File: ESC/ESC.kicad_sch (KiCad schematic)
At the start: 121 parts, among them J1 Screw_Terminal_01x02, J2 Conn_01x05, J3 Screw_Terminal_01x03, Q1 BS250, Q2 IPD031N03L, Q3 IPD031N03L, Q4 IPD031N03L, Q5 IPD031N03L, Q6 IPD031N03L, Q7 IPD031N03L, U1 LM7805_TO220, U2 DRV8302, U3 IR2101, U5 IR2101, U6 IR2101

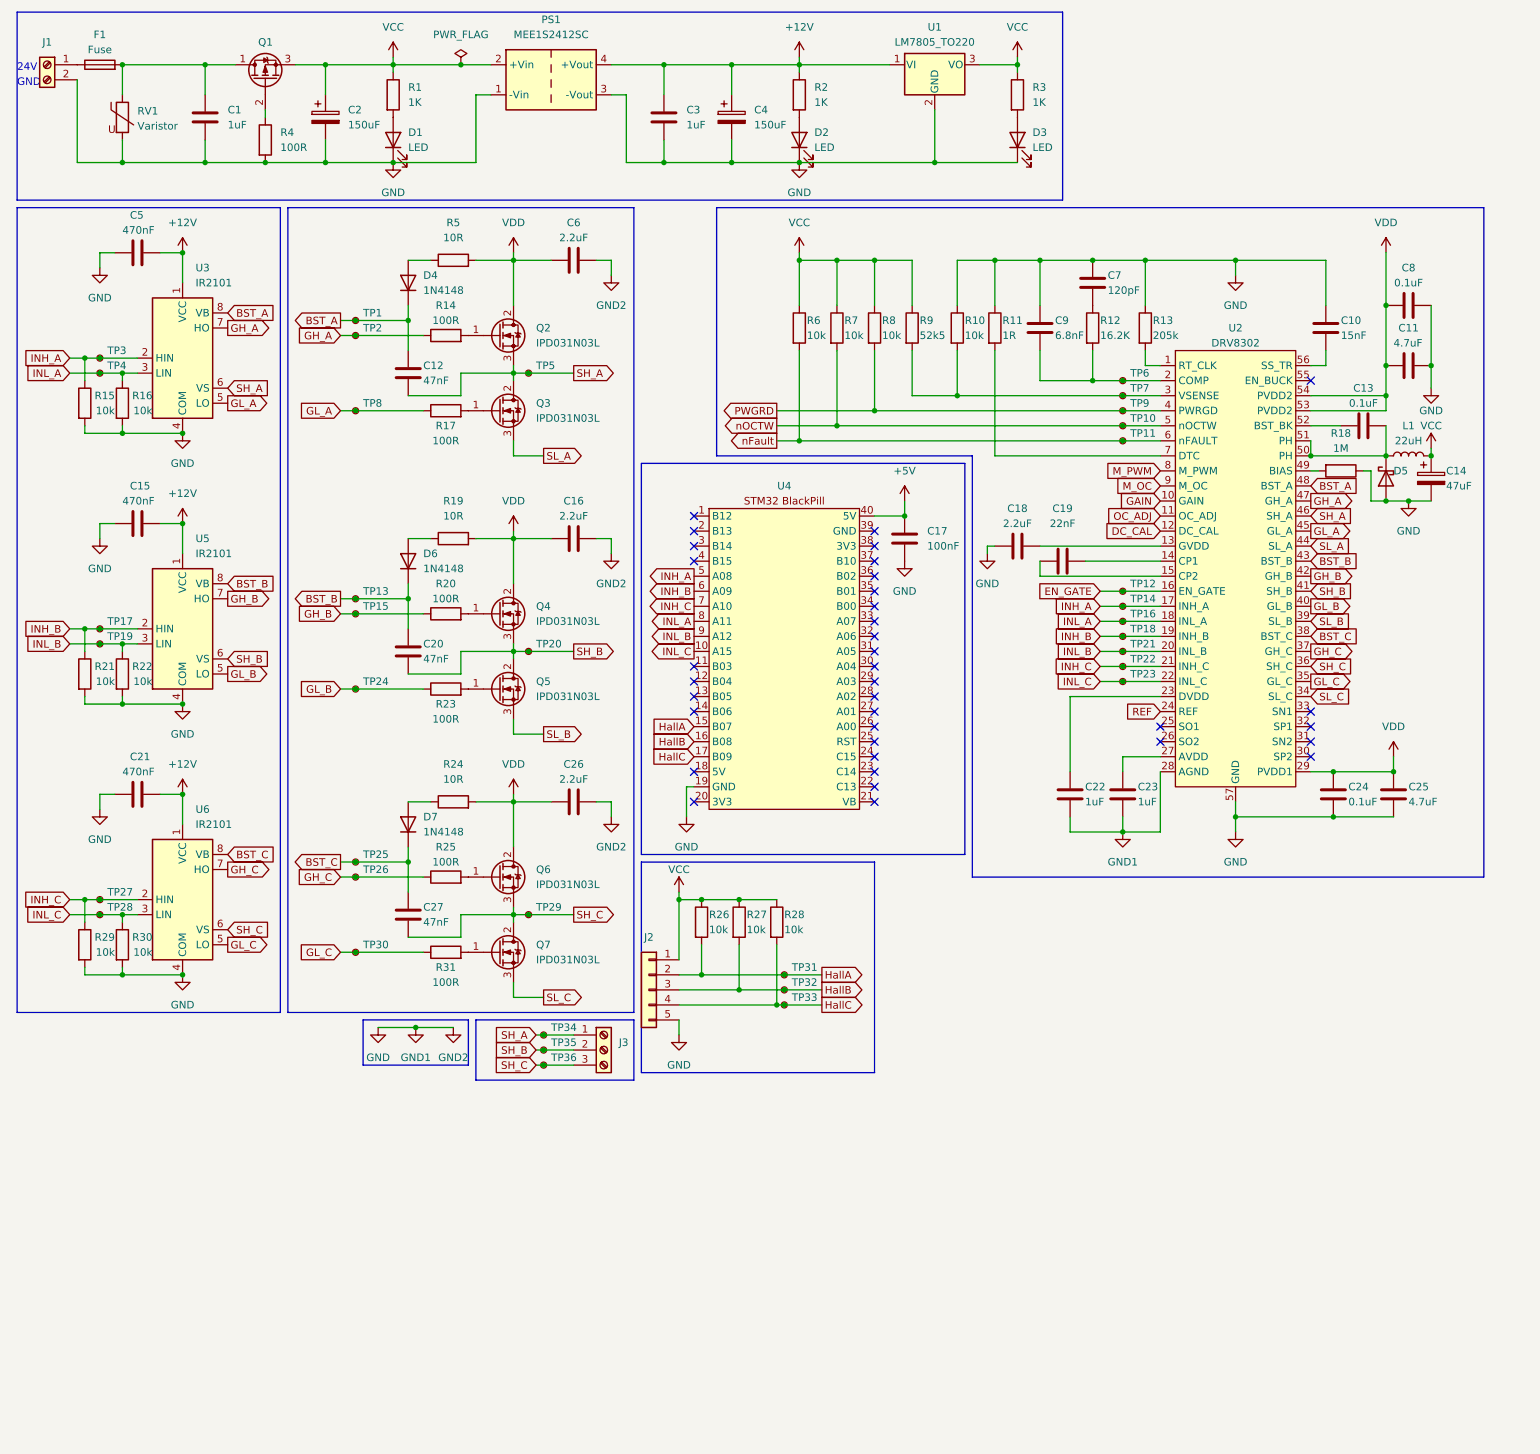
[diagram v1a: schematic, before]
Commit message: Added Connectors SPI and USART
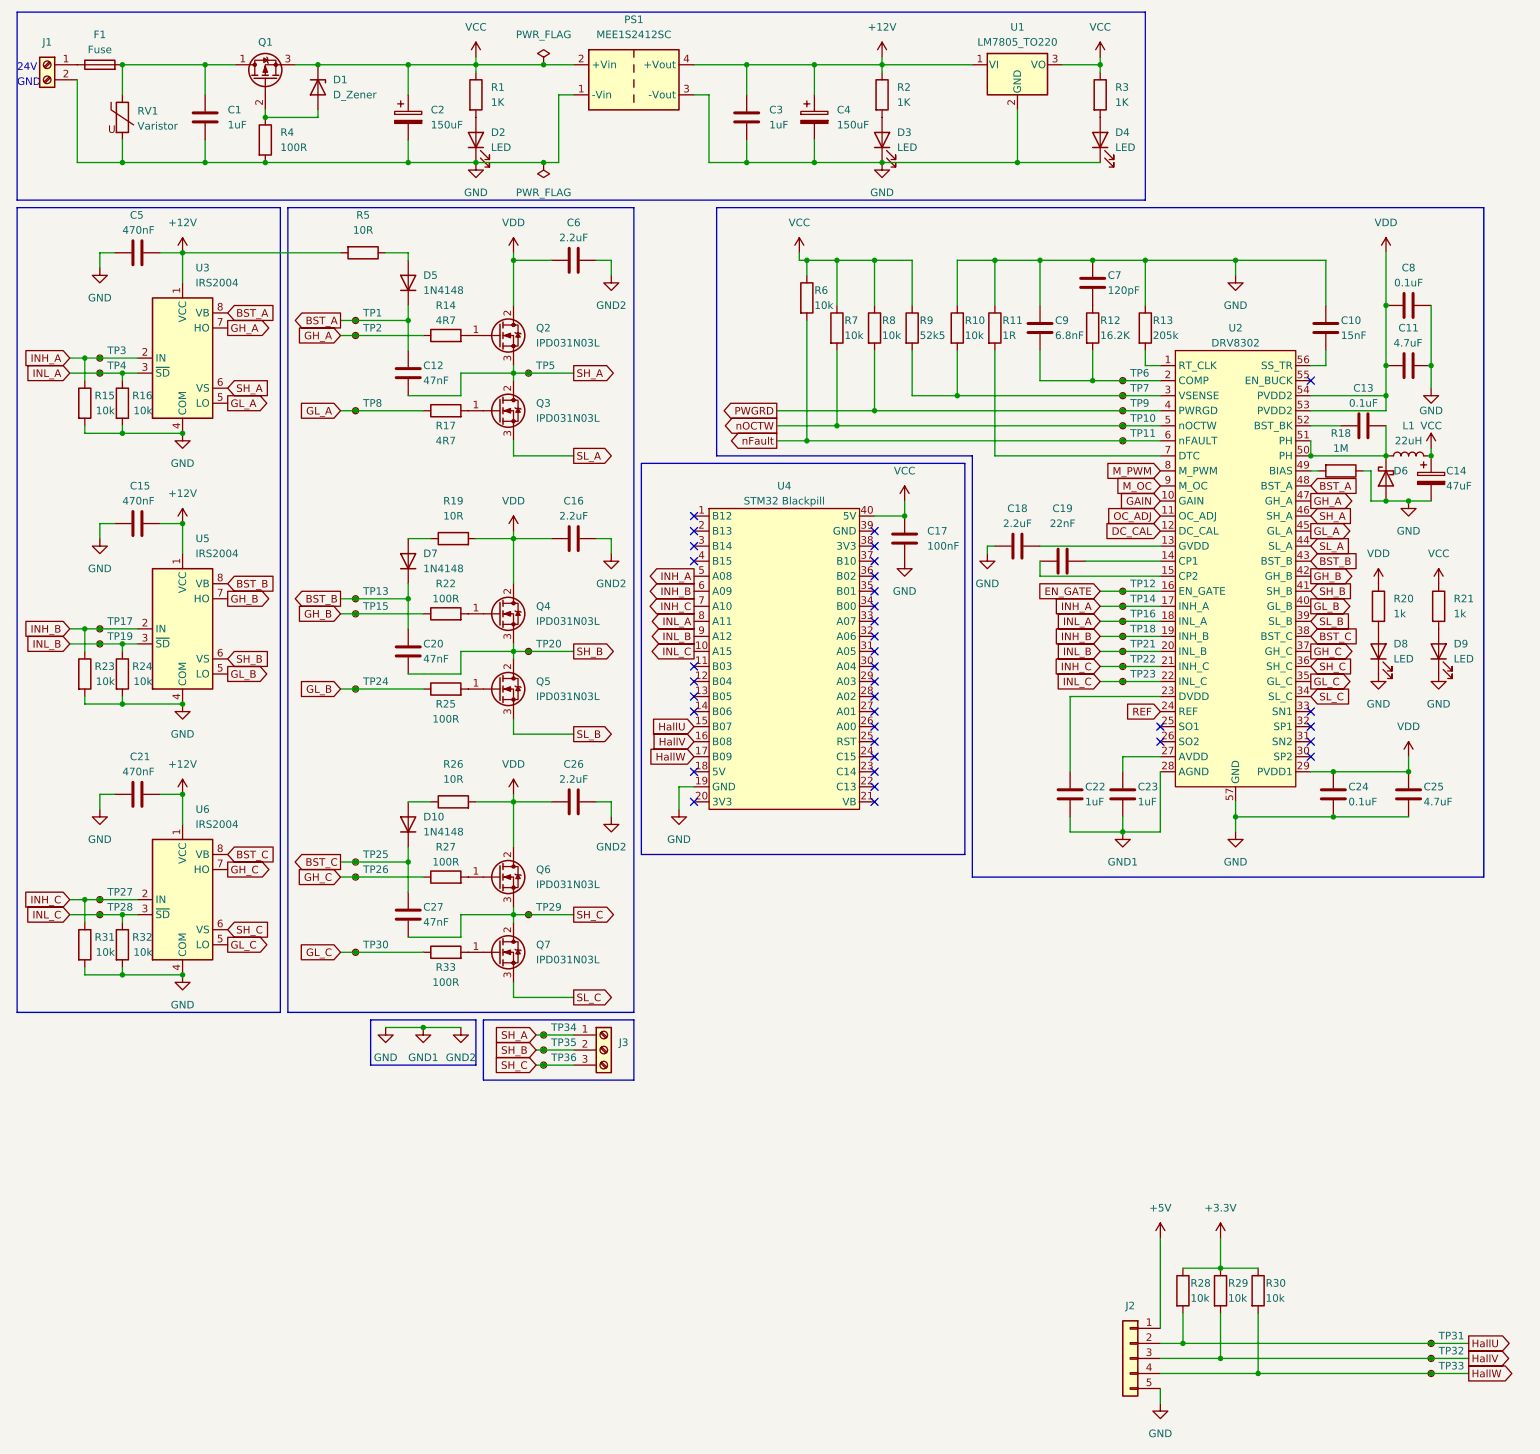
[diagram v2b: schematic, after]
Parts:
- removed U3, U5, U6: IR2101, symbol Driver_FET:IR2101
- added D1: D_Zener, symbol Device:D_Zener
- added D8, D9: LED, symbol Device:LED
- added R20, R21: 1k, Resistor_SMD:R_0603_1608Metric_Pad0.98x0.95mm_HandSolder, symbol Device:R
- added U3, U5, U6: IRS2004, symbol Driver_FET:IRS2004
- C1, C10, C11, C12, C13, C15, C16, C17, C18, C19, C20, C21, C22, C23, C24, C25, C26, C27, C3, C5, C6, C7, C8, C9: footprint (none) -> Capacitor_SMD:C_0603_1608Metric_Pad1.08x0.95mm_HandSolder
- C14, C2, C4: footprint (none) -> Capacitor_SMD:CP_Elec_6.3x7.7
- R1, R10, R11, R12, R13, R15, R16, R18, R19, R2, R3, R4, R5, R6, R7, R8, R9: footprint (none) -> Resistor_SMD:R_0603_1608Metric_Pad0.98x0.95mm_HandSolder
- R14, R17: value 100R -> 4R7; footprint (none) -> Resistor_SMD:R_0603_1608Metric_Pad0.98x0.95mm_HandSolder
- R22: renamed from R20; footprint (none) -> Resistor_SMD:R_0603_1608Metric_Pad0.98x0.95mm_HandSolder
- R23: renamed from R21; footprint (none) -> Resistor_SMD:R_0603_1608Metric_Pad0.98x0.95mm_HandSolder
- R24: renamed from R22; footprint (none) -> Resistor_SMD:R_0603_1608Metric_Pad0.98x0.95mm_HandSolder
- R25: renamed from R23; footprint (none) -> Resistor_SMD:R_0603_1608Metric_Pad0.98x0.95mm_HandSolder
- R26: renamed from R24; footprint (none) -> Resistor_SMD:R_0603_1608Metric_Pad0.98x0.95mm_HandSolder
- R27: renamed from R25; footprint (none) -> Resistor_SMD:R_0603_1608Metric_Pad0.98x0.95mm_HandSolder
- R28: renamed from R26; footprint (none) -> Resistor_SMD:R_0603_1608Metric_Pad0.98x0.95mm_HandSolder
- R29: renamed from R27; footprint (none) -> Resistor_SMD:R_0603_1608Metric_Pad0.98x0.95mm_HandSolder
- R30: renamed from R28; footprint (none) -> Resistor_SMD:R_0603_1608Metric_Pad0.98x0.95mm_HandSolder
- R31: renamed from R29; footprint (none) -> Resistor_SMD:R_0603_1608Metric_Pad0.98x0.95mm_HandSolder
- R32: renamed from R30; footprint (none) -> Resistor_SMD:R_0603_1608Metric_Pad0.98x0.95mm_HandSolder
- R33: renamed from R31; footprint (none) -> Resistor_SMD:R_0603_1608Metric_Pad0.98x0.95mm_HandSolder
- TP1, TP10, TP11, TP12, TP13, TP14, TP15, TP16, TP17, TP18, TP19, TP2, TP20, TP21, TP22, TP23, TP24, TP25, TP26, TP27, TP28, TP29, TP3, TP30, TP31, TP32, TP33, TP34, TP35, TP36, TP4, TP5, TP6, TP7, TP8, TP9: footprint (none) -> TestPoint:TestPoint_Pad_1.5x1.5mm
- U4: value ~ -> STM32 Blackpill
- renumbered D7 to D10, D1 to D2, D2 to D3, D3 to D4, D4 to D5, D5 to D6, D6 to D7
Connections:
- net +12V: now also R5.2, U3.1 (VCC), U5.1 (VCC), U6.1 (VCC)
- net +5V: now also J2.1 (Pin_1); no longer C17.1, U4.40 (5V)
- net BST_A: now also U3.8 (VB)
- net BST_B: now also U5.8 (VB)
- net BST_C: now also U6.8 (VB)
- net GH_A: now also U3.7 (HO)
- net GH_B: now also U5.7 (HO)
- net GH_C: now also U6.7 (HO)
- net GL_A: now also U3.5 (LO)
- net GL_B: now also U5.5 (LO)
- net GL_C: now also U6.5 (LO)
- net GND: now also D8.1 (K), D9.1 (K), U3.4 (COM), U5.4 (COM), U6.4 (COM)
- net INH_A: now also U3.2 (IN)
- net INH_B: now also U5.2 (IN)
- net INH_C: now also U6.2 (IN)
- net INL_A: now also U3.3 (~{SD})
- net INL_B: now also U5.3 (~{SD})
- net INL_C: now also U6.3 (~{SD})
- net SH_A: now also U3.6 (VS)
- net SH_B: now also U5.6 (VS)
- net SH_C: now also U6.6 (VS)
- net VCC: now also C17.1, U4.40 (5V), D1.1 (K), R21.1; no longer J2.1 (Pin_1), R28.1, R29.1, R30.1
- net VDD: now also R20.1; no longer R5.2
- net at Q1.2 (G), R4.1: now also D1.2 (A)
- net HallA renamed HallU
- net HallB renamed HallV
- net HallC renamed HallW
- new net: D9.2 (A), R21.2
- new net: D8.2 (A), R20.2
- new net +3.3V: R28.1, R29.1, R30.1
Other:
- moved on the sheet: C2, C25, C3, C4, D2, D3, D4, J2, PS1, R1, R2, R28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
